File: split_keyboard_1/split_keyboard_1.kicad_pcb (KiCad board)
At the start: 2 copper layers, 61 parts, among them SW1 SW_Push_45deg, SW10 SW_Push_45deg, SW11 SW_Push_45deg, SW12 SW_Push_45deg, SW13 SW_Push_45deg, SW14 SW_Push_45deg, SW15 SW_Push_45deg, SW16 SW_Push_45deg, SW17 SW_Push_45deg, SW18 SW_Push_45deg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

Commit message: on/off switch symbol and start on footprint
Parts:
- U1: footprint footprints:nice!nanoV2_reversible -> footprints:nice!nanoV2
- moved D25 228.5 mm to (45.0, 102.5), turned to 90 degrees
- moved D19 221.6 mm to (45.0, 85.7), turned to 90 degrees
- moved D13 215.1 mm to (45.0, 68.6), turned to 90 degrees
- moved D1 212.2 mm to (45.0, 34.5), turned to 90 degrees
- moved D26 211.2 mm to (63.0, 102.5), turned to 90 degrees
- moved D7 209.0 mm to (45.0, 51.6), turned to 90 degrees
- moved D20 204.1 mm to (63.0, 85.6), turned to 90 degrees
- moved D14 197.3 mm to (63.0, 68.5), turned to 90 degrees
- moved D27 194.1 mm to (81.0, 102.5), turned to 90 degrees
- moved D2 193.9 mm to (63.0, 34.5), turned to 90 degrees
- moved D8 191.0 mm to (63.0, 51.6), turned to 90 degrees
- moved D21 186.7 mm to (81.0, 85.5), turned to 90 degrees
- moved D9 179.8 mm to (81.0, 51.6), turned to 90 degrees
- moved D15 179.6 mm to (81.0, 68.5), turned to 90 degrees
- moved D28 177.3 mm to (99.0, 102.5), turned to 90 degrees
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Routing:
- net Col 0: track 0.00 -> 180.1 mm, vias 0 -> 5
- net Col 1: track 0.00 -> 165.0 mm, vias 0 -> 7
- net Row 4: track 0.00 -> 161.6 mm, vias 0 -> 6
- net Col 2: track 0.00 -> 149.8 mm, vias 0 -> 7
- net Row 3: track 0.00 -> 137.9 mm, vias 0 -> 4
- net Row 2: track 0.00 -> 120.3 mm, vias 0 -> 2
- net Col 3: track 0.00 -> 113.3 mm, vias 0 -> 9
- net Row 1: track 0.00 -> 104.8 mm, vias 0 -> 2
- net Col 4: track 0.00 -> 98.3 mm, vias 0 -> 7
- net Row 0: track 0.00 -> 94.9 mm
- net Col 5: track 0.00 -> 90.0 mm, vias 0 -> 7
- net GND: track 0.00 -> 28.4 mm, vias 0 -> 2
- net Net-(D19-A): track 0.00 -> 3.01 mm
- net Net-(D9-A): track 0.00 -> 2.96 mm
- net Net-(D8-A): track 0.00 -> 2.96 mm
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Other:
- board outline added: 111 x 89 mm

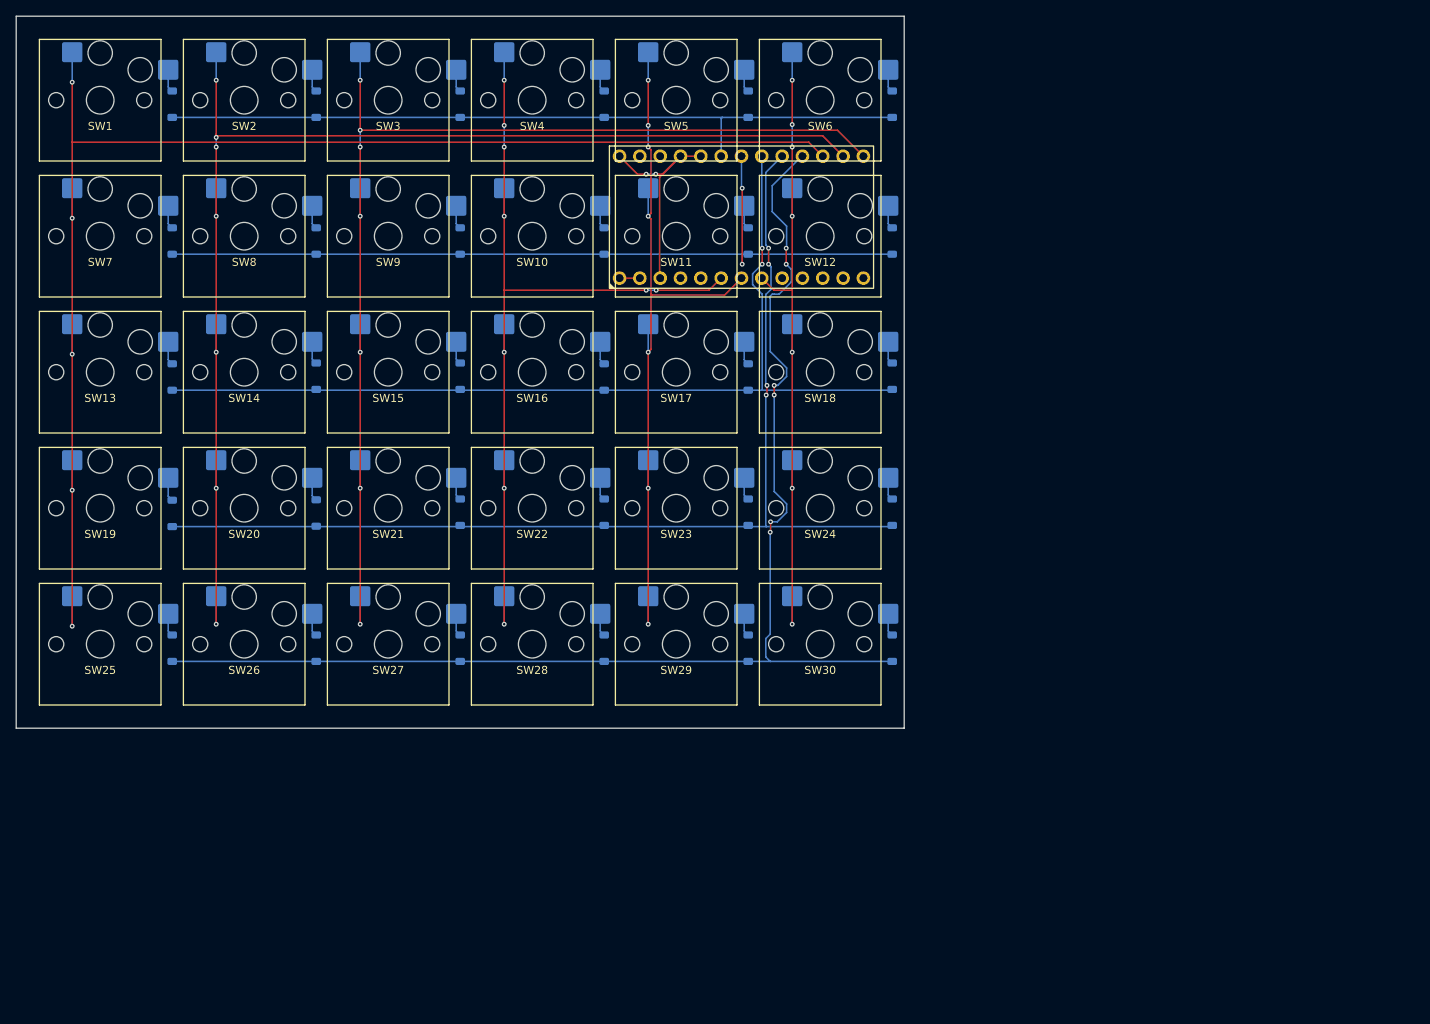
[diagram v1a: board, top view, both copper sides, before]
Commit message: Add reset and power switch
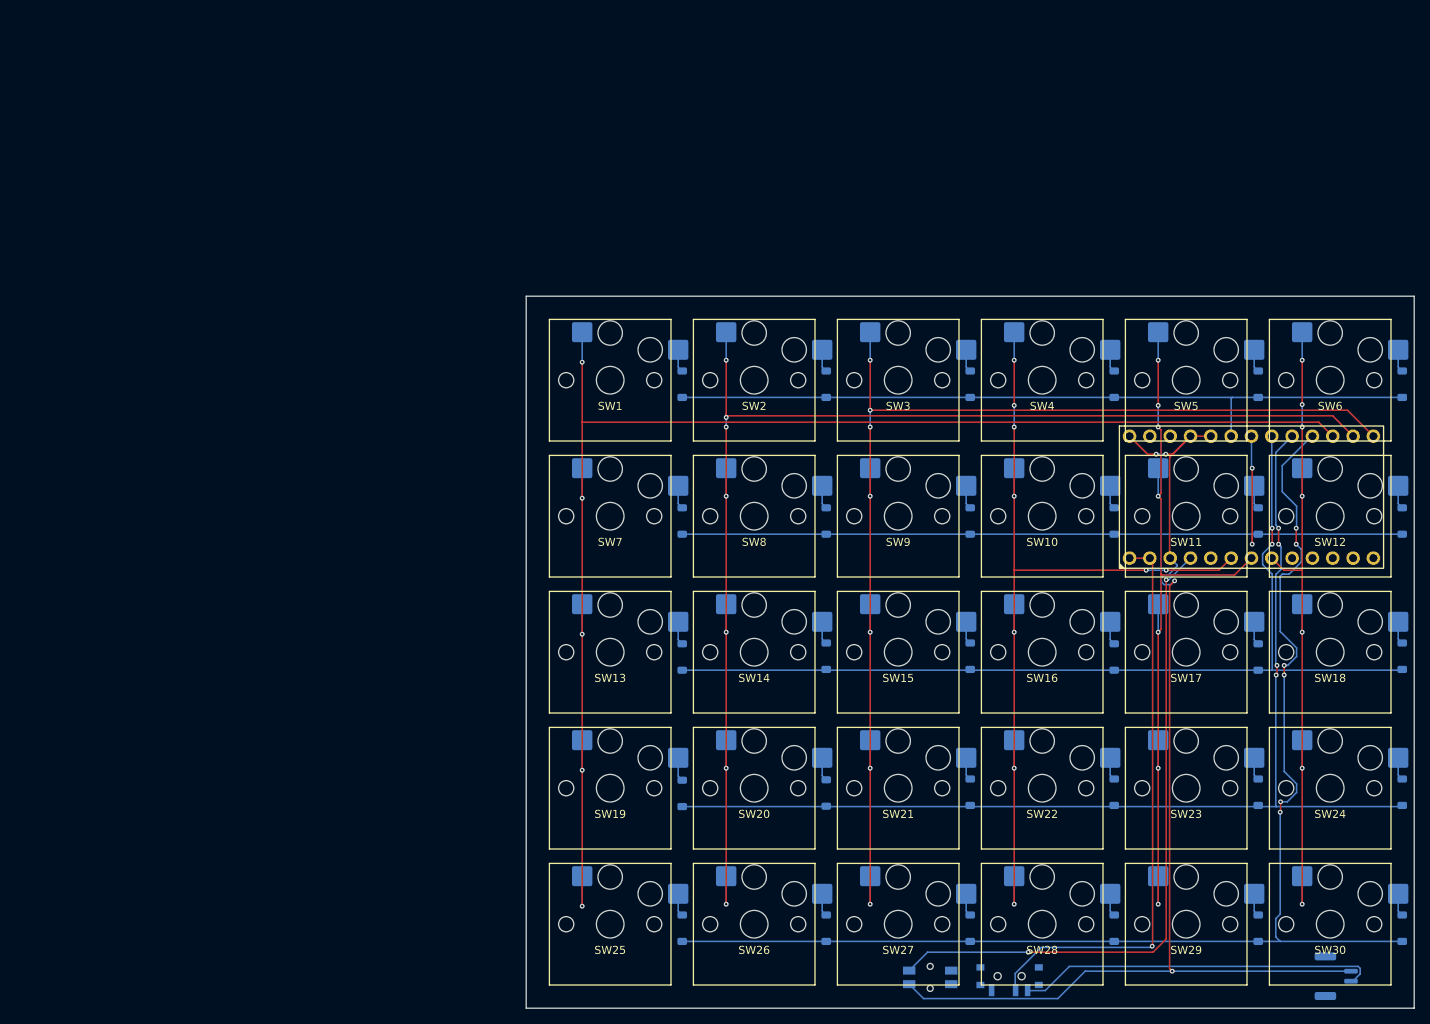
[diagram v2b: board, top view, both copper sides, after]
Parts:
- added J1: B2B-PH-SM4-TB, Connector_JST:JST_GH_SM02B-GHS-TB_1x02-1MP_P1.25mm_Horizontal, B.Cu at (190.5, 143.5)
- added SW31: ~, footprints:SSSS811101_SW_SPDT, B.Cu at (149.8, 143.4)
- added SW32: SW_Push, footprints:EVQPU_BTN, B.Cu at (139.8, 143.7)
- moved D1 72.7 mm to (108.8, 69.5)
- moved D13 72.7 mm to (108.8, 103.6)
- moved D14 72.7 mm to (126.8, 103.5)
- moved D15 72.7 mm to (144.8, 103.5)
- moved D16 72.7 mm to (162.8, 103.6)
- moved D17 72.7 mm to (180.8, 103.6)
- moved D18 72.7 mm to (198.8, 103.5)
- moved D19 72.7 mm to (108.8, 120.7)
- moved D2 72.7 mm to (126.8, 69.5)
- moved D20 72.7 mm to (126.8, 120.6)
- moved D21 72.7 mm to (144.8, 120.5)
- moved D22 72.7 mm to (162.8, 120.5)
- moved D23 72.7 mm to (180.8, 120.5)
- moved D24 72.7 mm to (198.8, 120.5)
- moved D25 72.7 mm to (108.8, 137.5)
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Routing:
- net GND: track 28.4 -> 141.4 mm, vias 2 -> 4
- net Net-(U1-RESET): track 0.00 -> 82.8 mm, vias 0 -> 2
- net Net-(SW31-C): track 2.54 -> 71.9 mm, vias 0 -> 1
- net Net-(SW31-B): track 0.00 -> 45.2 mm
